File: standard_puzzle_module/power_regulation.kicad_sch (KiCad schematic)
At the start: 9 parts, among them J10 Screw_Terminal_01x02, U9 TSR2-2450

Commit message: chore: clean up
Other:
- title: Power input and regulation (12V to 5V) -> Power input and regulation
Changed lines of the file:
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@@
 	(paper "A4")
 	(title_block
-		(title "Power input and regulation (12V to 5V)")
+		(title "Power input and regulation")
 	)
 	(junction
@@
 	)
 	(junction
+		(at 101.6 87.63)
+		(diameter 0)
+		(color 0 0 0 0)
+	)
+	(junction
 		(at 147.32 82.55)
 		(diameter 0)
@@
 	(wire
 		(pts
-			(xy 101.6 82.55) (xy 101.6 92.71)
+			(xy 101.6 82.55) (xy 101.6 87.63)
 		)
 		(stroke
@@
 	(wire
 		(pts
+			(xy 101.6 87.63) (xy 101.6 92.71)
+		)
+		(stroke
+			(width 0)
+			(type default)
+		)
+	)
+	(wire
+		(pts
 			(xy 147.32 93.98) (xy 147.32 106.68)
 		)
@@
 	)
 	(label "Power input and regulation (12V to 5V)"
-		(at 123.19 73.66 0)
+		(at 123.19 71.12 0)
 		(effects
 			(font
 				(size 1.778 1.778)
-			)
-			(justify left bottom)
-		)
-	)
-	(label "+12V"
-		(at 101.6 90.17 0)
-		(effects
-			(font
-				(size 1.27 1.27)
-			)
-			(justify left bottom)
-		)
-	)
-	(label "GND"
-		(at 101.6 99.06 0)
-		(effects
-			(font
-				(size 1.27 1.27)
 			)
 			(justify left bottom)
@@
 					(unit 1)
 				)
+			)
+		)
+	)
+	(symbol
+		(lib_id "power:+12V")
+		(at 101.6 87.63 0)
+		(unit 1)
+		(body_style 1)
+		(exclude_from_sim no)
+		(in_bom yes)
+		(on_board yes)
+		(in_pos_files yes)
+		(dnp no)
+		(fields_autoplaced yes)
+		(property "Reference" "#PWR04"
+			(at 101.6 91.44 0)
+			(hide yes)
+			(show_name no)
+			(do_not_autoplace no)
+			(effects
+				(font
+					(size 1.27 1.27)
+				)
+			)
+		)
+		(property "Value" "+12V"
+			(at 101.6 82.55 0)
+			(show_name no)
+			(do_not_autoplace no)
+			(effects
+				(font
+					(size 1.27 1.27)
+				)
+			)
+		)
+		(property "Footprint" ""
+			(at 101.6 87.63 0)
+			(hide yes)
+			(show_name no)
+			(do_not_autoplace no)
+			(effects
+				(font
+					(size 1.27 1.27)
+				)
+			)
+		)
+		(property "Datasheet" ""
+			(at 101.6 87.63 0)
+			(hide yes)
+			(show_name no)
+			(do_not_autoplace no)
+			(effects
+				(font
+					(size 1.27 1.27)
+				)
+			)
+		)
+		(property "Description" "Power symbol creates a global label with name \"+12V\""
+			(at 101.6 87.63 0)
+			(hide yes)
+			(show_name no)
+			(do_not_autoplace no)
+			(effects
+				(font
+					(size 1.27 1.27)
+				)
+			)
+		)
+		(pin "1"
+		)
+		(instances
+			(project "standard_puzzle_box"
+				(path "/13314f97-080e-4924-a8fe-b4d224920625/84527307-db04-4e9a-b4c6-f367c646187b"
+					(reference "#PWR04")
+					(unit 1)
+				)

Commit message: feat: unscrew git tracking
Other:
- moved on the sheet: C15, C16
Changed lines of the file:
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@@
+	)
+	(junction
+		(at 191.77 82.55)
+		(diameter 0)
+		(color 0 0 0 0)
+	)
+	(junction
+		(at 135.89 106.68)
+		(diameter 0)
+		(color 0 0 0 0)
+	)
+	(junction
+		(at 182.88 106.68)
+		(diameter 0)
+		(color 0 0 0 0)
 	)
 	(junction
@@
 	)
 	(junction
-		(at 135.89 106.68)
-		(diameter 0)
-		(color 0 0 0 0)
-	)
-	(junction
-		(at 182.88 106.68)
-		(diameter 0)
-		(color 0 0 0 0)
-	)
-	(junction
 		(at 101.6 87.63)
 		(diameter 0)
@@
 	)
 	(junction
+		(at 191.77 106.68)
+		(diameter 0)
+		(color 0 0 0 0)
+	)
+	(junction
 		(at 182.88 82.55)
 		(diameter 0)
@@
 	)
 	(junction
-		(at 191.77 82.55)
-		(diameter 0)
-		(color 0 0 0 0)
-	)
-	(junction
 		(at 115.57 106.68)
 		(diameter 0)
@@
 	)
 	(junction
-		(at 191.77 106.68)
-		(diameter 0)
-		(color 0 0 0 0)
-	)
-	(junction
 		(at 168.91 106.68)
 		(diameter 0)
@@
 	(wire
 		(pts
-			(xy 191.77 102.87) (xy 191.77 106.68)
+			(xy 191.77 101.6) (xy 191.77 106.68)
 		)
 		(stroke
@@
 	(wire
 		(pts
-			(xy 182.88 92.71) (xy 182.88 106.68)
+			(xy 182.88 93.98) (xy 182.88 106.68)
 		)
 		(stroke
@@
 	(wire
 		(pts
-			(xy 191.77 95.25) (xy 191.77 82.55)
+			(xy 191.77 93.98) (xy 191.77 82.55)
 		)
 		(stroke
@@
 	(wire
 		(pts
-			(xy 182.88 82.55) (xy 182.88 85.09)
+			(xy 182.88 82.55) (xy 182.88 86.36)
 		)
 		(stroke
@@
 	(symbol
 		(lib_id "Device:C_Polarized")
-		(at 182.88 88.9 0)
+		(at 182.88 90.17 0)
 		(unit 1)
 		(body_style 1)
@@
 		(fields_autoplaced yes)
 		(property "Reference" "C15"
-			(at 186.69 86.7409 0)
+			(at 186.69 88.0109 0)
 			(show_name no)
 			(do_not_autoplace no)
@@
 		)
 		(property "Value" "47uF"
-			(at 186.69 89.2809 0)
+			(at 186.69 90.5509 0)
 			(show_name no)
 			(do_not_autoplace no)
@@
 		)
 		(property "Footprint" ""
-			(at 183.8452 92.71 0)
+			(at 183.8452 93.98 0)
 			(hide yes)
 			(show_name no)
@@
 		)
 		(property "Datasheet" ""
-			(at 182.88 88.9 0)
+			(at 182.88 90.17 0)
 			(hide yes)
 			(show_name no)
@@
 		)
 		(property "Description" "Polarized capacitor"
-			(at 182.88 88.9 0)
+			(at 182.88 90.17 0)
 			(hide yes)
 			(show_name no)
@@
 	(symbol
 		(lib_id "Device:C")
-		(at 191.77 99.06 0)
+		(at 191.77 97.79 0)
 		(unit 1)
 		(body_style 1)
@@
 		(fields_autoplaced yes)
 		(property "Reference" "C16"
-			(at 195.58 97.7899 0)
+			(at 195.58 96.5199 0)
 			(show_name no)
 			(do_not_autoplace no)
@@
 		)
 		(property "Value" "100nF"
-			(at 195.58 100.3299 0)
+			(at 195.58 99.0599 0)
 			(show_name no)
 			(do_not_autoplace no)
@@
 		)
 		(property "Footprint" ""
-			(at 192.7352 102.87 0)
+			(at 192.7352 101.6 0)
 			(hide yes)
 			(show_name no)
@@
 		)
 		(property "Datasheet" ""
-			(at 191.77 99.06 0)
+			(at 191.77 97.79 0)
 			(hide yes)
 			(show_name no)
@@
 		)
 		(property "Description" "Unpolarized capacitor"
-			(at 191.77 99.06 0)
-			(hide yes)
-			(show_name no)
+			(at 191.77 97.79 0)
+			(hide yes)
+			(show_name no)

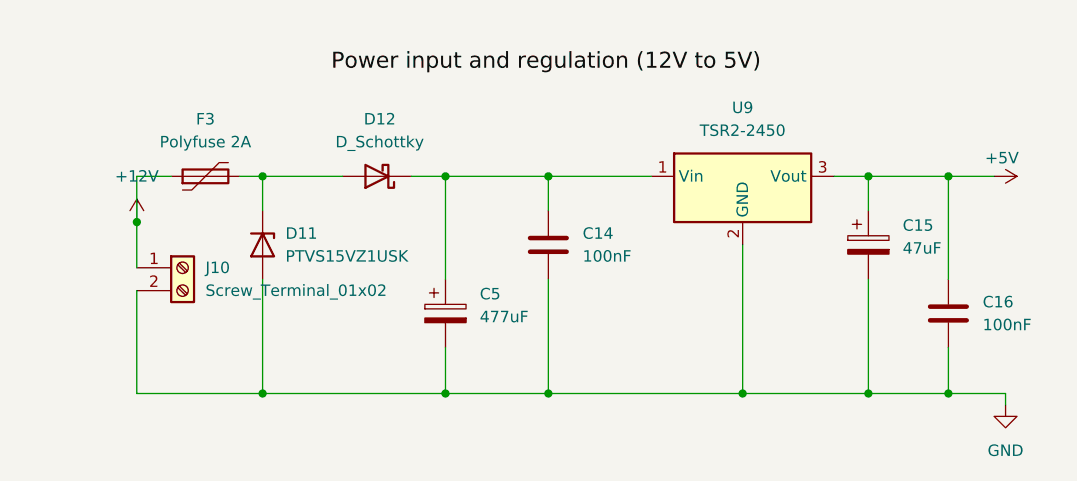
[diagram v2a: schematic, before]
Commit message: feat: clean up schematic references and run clean annotation
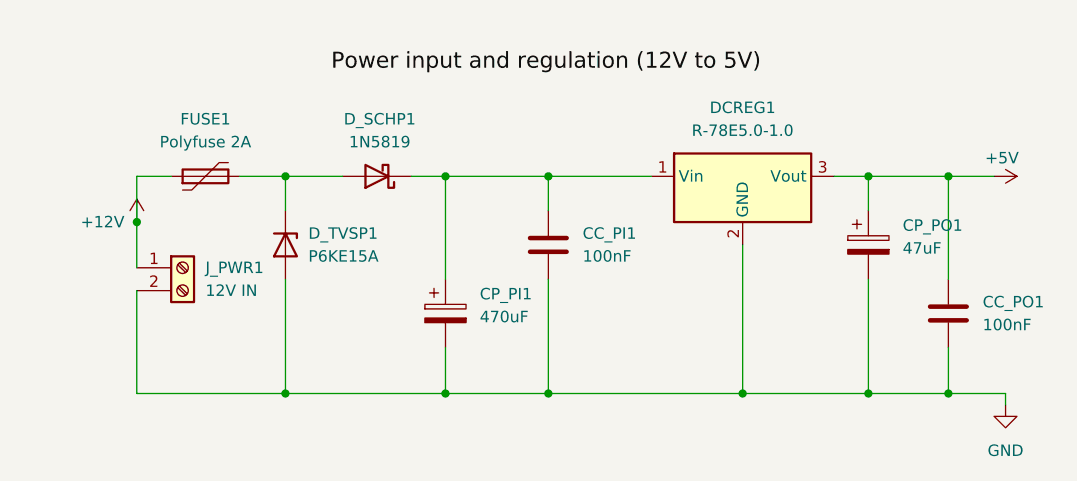
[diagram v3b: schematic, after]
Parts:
- CC_PI1: renamed from C14; footprint (none) -> Capacitor_THT:C_Disc_D5.0mm_W2.5mm_P5.00mm
- CC_PO1: renamed from C16; footprint (none) -> Capacitor_THT:C_Disc_D5.0mm_W2.5mm_P5.00mm
- CP_PI1: renamed from C5; value 477uF -> 470uF; footprint (none) -> Capacitor_THT:CP_Radial_D10.0mm_P5.00mm
- CP_PO1: renamed from C15; footprint (none) -> Capacitor_THT:CP_Radial_D6.3mm_P2.50mm
- DCREG1: renamed from U9; value TSR2-2450 -> R-78E5.0-1.0; footprint Converter_DCDC:Converter_DCDC_TRACO_TSR2-xxxx_THT -> Converter_DCDC:Converter_DCDC_RECOM_R-78E-0.5_THT
- D_SCHP1: renamed from D12; value D_Schottky -> 1N5819; footprint (none) -> Diode_THT:D_DO-35_SOD27_P7.62mm_Horizontal
- D_TVSP1: renamed from D11; value PTVS15VZ1USK -> P6KE15A; footprint Diode_SMD:Nexperia_DSN1608-2_1.6x0.8mm -> Diode_THT:D_DO-15_P12.70mm_Horizontal
- FUSE1: renamed from F3; footprint (none) -> Fuse:Fuse_BelFuse_0ZRE0040FF_L11.5mm_W3.8mm
- J_PWR1: renamed from J10; value Screw_Terminal_01x02 -> 12V IN; footprint (none) -> TerminalBlock_Phoenix:TerminalBlock_Phoenix_MKDS-1,5-2-5.08_1x02_P5.08mm_Horizontal
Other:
- moved on the sheet: D_TVSP1
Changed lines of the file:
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@@
-	)
-	(junction
-		(at 115.57 82.55)
-		(diameter 0)
-		(color 0 0 0 0)
 	)
 	(junction
@@
 	)
 	(junction
-		(at 115.57 106.68)
+		(at 118.11 106.68)
 		(diameter 0)
 		(color 0 0 0 0)
@@
 		(color 0 0 0 0)
 	)
+	(junction
+		(at 118.11 82.55)
+		(diameter 0)
+		(color 0 0 0 0)
+	)
 	(wire
 		(pts
@@
 	(wire
 		(pts
-			(xy 113.03 82.55) (xy 115.57 82.55)
-		)
-		(stroke
-			(width 0)
-			(type default)
-		)
-	)
-	(wire
-		(pts
-			(xy 115.57 106.68) (xy 135.89 106.68)
+			(xy 113.03 82.55) (xy 118.11 82.55)
 		)
 		(stroke
@@
 	(wire
 		(pts
-			(xy 101.6 106.68) (xy 115.57 106.68)
+			(xy 101.6 106.68) (xy 118.11 106.68)
 		)
 		(stroke
@@
 	(wire
 		(pts
-			(xy 115.57 93.98) (xy 115.57 106.68)
+			(xy 118.11 93.98) (xy 118.11 106.68)
 		)
 		(stroke
@@
 	(wire
 		(pts
+			(xy 118.11 82.55) (xy 124.46 82.55)
+		)
+		(stroke
+			(width 0)
+			(type default)
+		)
+	)
+	(wire
+		(pts
 			(xy 168.91 106.68) (xy 182.88 106.68)
 		)
@@
 	(wire
 		(pts
-			(xy 115.57 82.55) (xy 115.57 86.36)
+			(xy 118.11 82.55) (xy 118.11 86.36)
 		)
 		(stroke
@@
 	(wire
 		(pts
-			(xy 115.57 82.55) (xy 124.46 82.55)
+			(xy 118.11 106.68) (xy 135.89 106.68)
 		)
 		(stroke
@@
 		(dnp no)
 		(fields_autoplaced yes)
-		(property "Reference" "C14"
+		(property "Reference" "CC_PI1"
 			(at 151.13 88.8999 0)
 			(show_name no)
@@
 			)
 		)
-		(property "Footprint" ""
+		(property "Footprint" "Capacitor_THT:C_Disc_D5.0mm_W2.5mm_P5.00mm"
 			(at 148.2852 93.98 0)
 			(hide yes)
@@
 			(project "standard_puzzle_box"
 				(path "/13314f97-080e-4924-a8fe-b4d224920625/84527307-db04-4e9a-b4c6-f367c646187b"
-					(reference "C14")
+					(reference "CC_PI1")
 					(unit 1)
 				)
@@
 		(dnp no)
 		(fields_autoplaced yes)
-		(property "Reference" "C15"
+		(property "Reference" "CP_PO1"
 			(at 186.69 88.0109 0)
 			(show_name no)
@@
 			)
 		)
-		(property "Footprint" ""
+		(property "Footprint" "Capacitor_THT:CP_Radial_D6.3mm_P2.50mm"
 			(at 183.8452 93.98 0)
 			(hide yes)
@@
 			(project "standard_puzzle_box"
 				(path "/13314f97-080e-4924-a8fe-b4d224920625/84527307-db04-4e9a-b4c6-f367c646187b"
-					(reference "C15")
+					(reference "CP_PO1")
 					(unit 1)
 				)
@@
 	(symbol
 		(lib_id "Diode:PTVS15VZ1USK")
-		(at 115.57 90.17 270)
+		(at 118.11 90.17 270)
 		(unit 1)
 		(body_style 1)
@@
 		(dnp no)
 		(fields_autoplaced yes)
-		(property "Reference" "D11"
-			(at 118.11 88.8999 90)
-			(show_name no)
-			(do_not_autoplace no)
-			(effects
-				(font
-					(size 1.27 1.27)
-				)
-				(justify left)
-			)
-		)
-		(property "Value" "PTVS15VZ1USK"
-			(at 118.11 91.4399 90)
-			(show_name no)
-			(do_not_autoplace no)
-			(effects
-				(font
-					(size 1.27 1.27)
-				)
-				(justify left)
-			)
-		)
-		(property "Footprint" "Diode_SMD:Nexperia_DSN1608-2_1.6x0.8mm"
-			(at 111.125 90.17 0)
+		(property "Reference" "D_TVSP1"
+			(at 120.65 88.8999 90)
+			(show_name no)
+			(do_not_autoplace no)
+			(effects
+				(font
+					(size 1.27 1.27)
+				)
+				(justify left)
+			)
+		)
+		(property "Value" "P6KE15A"
+			(at 120.65 91.4399 90)
+			(show_name no)
+			(do_not_autoplace no)
+			(effects
+				(font
+					(size 1.27 1.27)
+				)
+				(justify left)
+			)
+		)
+		(property "Footprint" "Diode_THT:D_DO-15_P12.70mm_Horizontal"
+			(at 113.665 90.17 0)
 			(hide yes)
 			(show_name no)
@@
 		)
 		(property "Datasheet" "https://assets.nexperia.com/documents/data-sheet/PTVS15VZ1USK.pdf"
-			(at 115.57 90.17 0)
+			(at 118.11 90.17 0)
 			(hide yes)
 			(show_name no)
@@
 		)
 		(property "Description" "15V, 1900W TVS unidirectional diode, DSN1608-2"
-			(at 115.57 90.17 0)
+			(at 118.11 90.17 0)
 			(hide yes)
 			(show_name no)
@@
 			(project "standard_puzzle_box"
 				(path "/13314f97-080e-4924-a8fe-b4d224920625/84527307-db04-4e9a-b4c6-f367c646187b"
-					(reference "D11")
+					(reference "D_TVSP1")
 					(unit 1)
 				)
@@
 		(in_pos_files yes)
 		(dnp no)
-		(fields_autoplaced yes)
 		(property "Reference" "#PWR04"
 			(at 101.6 91.44 0)
@@
 		)
 		(property "Value" "+12V"
-			(at 101.6 82.55 0)
+			(at 97.79 87.63 0)
 			(show_name no)
 			(do_not_autoplace no)
@@
 		(dnp no)
 		(fields_autoplaced yes)
-		(property "Reference" "U9"
+		(property "Reference" "DCREG1"
 			(at 168.91 74.93 0)
 			(show_name no)
@@
 			)
 		)
-		(property "Value" "TSR2-2450"
+		(property "Value" "R-78E5.0-1.0"
 			(at 168.91 77.47 0)
 			(show_name no)
@@
 			)
 		)
-		(property "Footprint" "Converter_DCDC:Converter_DCDC_TRACO_TSR2-xxxx_THT"
+		(property "Footprint" "Converter_DCDC:Converter_DCDC_RECOM_R-78E-0.5_THT"
 			(at 168.91 91.186 0)
 			(hide yes)
@@
 			(project "standard_puzzle_box"
 				(path "/13314f97-080e-4924-a8fe-b4d224920625/84527307-db04-4e9a-b4c6-f367c646187b"
-					(reference "U9")
+					(reference "DCREG1")
 					(unit 1)
 				)
@@
 		(dnp no)
 		(fields_autoplaced yes)
-		(property "Reference" "C16"
+		(property "Reference" "CC_PO1"
 			(at 195.58 96.5199 0)
 			(show_name no)
@@
 			)
 		)
-		(property "Footprint" ""
+		(property "Footprint" "Capacitor_THT:C_Disc_D5.0mm_W2.5mm_P5.00mm"
 			(at 192.7352 101.6 0)
 			(hide yes)
@@
 			(project "standard_puzzle_box"
 				(path "/13314f97-080e-4924-a8fe-b4d224920625/84527307-db04-4e9a-b4c6-f367c646187b"
-					(reference "C16")
+					(reference "CC_PO1")
 					(unit 1)
 				)
@@
 		(dnp no)
 		(fields_autoplaced yes)
-		(property "Reference" "D12"
+		(property "Reference" "D_SCHP1"
 			(at 128.5875 76.2 0)
 			(show_name no)
@@
 			)
 		)
-		(property "Value" "D_Schottky"
+		(property "Value" "1N5819"
 			(at 128.5875 78.74 0)
 			(show_name no)
@@
 			)
 		)
-		(property "Footprint" ""
+		(property "Footprint" "Diode_THT:D_DO-35_SOD27_P7.62mm_Horizontal"
 			(at 128.27 82.55 0)
 			(hide yes)
@@
 			(project "standard_puzzle_box"
 				(path "/13314f97-080e-4924-a8fe-b4d224920625/84527307-db04-4e9a-b4c6-f367c646187b"
-					(reference "D12")
+					(reference "D_SCHP1")
 					(unit 1)
 				)
@@
 		(dnp no)
 		(fields_autoplaced yes)
-		(property "Reference" "F3"
+		(property "Reference" "FUSE1"
 			(at 109.22 76.2 90)
 			(show_name no)
@@
 			)
 		)
-		(property "Footprint" ""
+		(property "Footprint" "Fuse:Fuse_BelFuse_0ZRE0040FF_L11.5mm_W3.8mm"
 			(at 114.3 81.28 0)
 			(hide yes)
@@
 			(project "standard_puzzle_box"
 				(path "/13314f97-080e-4924-a8fe-b4d224920625/84527307-db04-4e9a-b4c6-f367c646187b"
-					(reference "F3")
+					(reference "FUSE1")
 					(unit 1)
 				)
@@
 		(dnp no)
 		(fields_autoplaced yes)
-		(property "Reference" "J10"
+		(property "Reference" "J_PWR1"
 			(at 109.22 92.7099 0)
 			(show_name no)
@@
 			)
 		)
-		(property "Value" "Screw_Terminal_01x02"
+		(property "Value" "12V IN"
 			(at 109.22 95.2499 0)
 			(show_name no)
@@
 			)
 		)
-		(property "Footprint" ""
+		(property "Footprint" "TerminalBlock_Phoenix:TerminalBlock_Phoenix_MKDS-1,5-2-5.08_1x02_P5.08mm_Horizontal"
 			(at 106.68 92.71 0)
 			(hide yes)
@@
 			(project "standard_puzzle_box"
 				(path "/13314f97-080e-4924-a8fe-b4d224920625/84527307-db04-4e9a-b4c6-f367c646187b"
-					(reference "J10")
+					(reference "J_PWR1")
 					(unit 1)
 				)
@@
 		(dnp no)
 		(fields_autoplaced yes)
-		(property "Reference" "C5"
+		(property "Reference" "CP_PI1"
 			(at 139.7 95.6309 0)
 			(show_name no)
@@
 			)
 		)
-		(property "Value" "477uF"
+		(property "Value" "470uF"
 			(at 139.7 98.1709 0)
 			(show_name no)
@@
 			)
 		)
-		(property "Footprint" ""
+		(property "Footprint" "Capacitor_THT:CP_Radial_D10.0mm_P5.00mm"
 			(at 136.8552 101.6 0)
 			(hide yes)
@@
 			(project "standard_puzzle_box"
 				(path "/13314f97-080e-4924-a8fe-b4d224920625/84527307-db04-4e9a-b4c6-f367c646187b"
-					(reference "C5")
+					(reference "CP_PI1")
 					(unit 1)
 				)

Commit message: fix: run erc and fix errors and warnings
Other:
- note added: "Power input and regulation (12V to 5V)"

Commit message: feat: salvaging stuff after lossy crash
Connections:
- net +12V: now also CC_PI1.1, CP_PI1.1, DCREG1.1 (Vin), D_SCHP1.1 (K); no longer FUSE1.1, J_PWR1.1 (Pin_1)
- new net: FUSE1.1, J_PWR1.1 (Pin_1)
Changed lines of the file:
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@@
+	)
+	(junction
+		(at 152.4 82.55)
+		(diameter 0)
+		(color 0 0 0 0)
 	)
 	(junction
@@
 	)
 	(junction
-		(at 101.6 87.63)
+		(at 147.32 82.55)
 		(diameter 0)
 		(color 0 0 0 0)
@@
 	)
 	(junction
-		(at 147.32 82.55)
-		(diameter 0)
-		(color 0 0 0 0)
-	)
-	(junction
 		(at 198.12 106.68)
 		(diameter 0)
@@
 	(wire
 		(pts
+			(xy 147.32 82.55) (xy 152.4 82.55)
+		)
+		(stroke
+			(width 0)
+			(type default)
+		)
+	)
+	(wire
+		(pts
 			(xy 182.88 106.68) (xy 191.77 106.68)
 		)
@@
 	(wire
 		(pts
-			(xy 101.6 82.55) (xy 101.6 87.63)
-		)
-		(stroke
-			(width 0)
-			(type default)
-		)
-	)
-	(wire
-		(pts
-			(xy 147.32 82.55) (xy 154.94 82.55)
+			(xy 101.6 82.55) (xy 101.6 92.71)
 		)
 		(stroke
@@
 	(wire
 		(pts
-			(xy 101.6 87.63) (xy 101.6 92.71)
-		)
-		(stroke
-			(width 0)
-			(type default)
-		)
-	)
-	(wire
-		(pts
 			(xy 147.32 93.98) (xy 147.32 106.68)
 		)
@@
 		(pts
 			(xy 179.07 82.55) (xy 182.88 82.55)
+		)
+		(stroke
+			(width 0)
+			(type default)
+		)
+	)
+	(wire
+		(pts
+			(xy 152.4 82.55) (xy 154.94 82.55)
 		)
 		(stroke
@@
 	(symbol
 		(lib_id "power:+12V")
-		(at 101.6 87.63 0)
+		(at 152.4 82.55 0)
 		(unit 1)
 		(body_style 1)
@@
 		(dnp no)
 		(property "Reference" "#PWR04"
-			(at 101.6 91.44 0)
+			(at 152.4 86.36 0)
 			(hide yes)
 			(show_name no)
@@
 		)
 		(property "Value" "+12V"
-			(at 97.79 87.63 0)
+			(at 148.59 80.01 0)
 			(show_name no)
 			(do_not_autoplace no)
@@
 		)
 		(property "Footprint" ""
-			(at 101.6 87.63 0)
+			(at 152.4 82.55 0)
 			(hide yes)
 			(show_name no)
@@
 		)
 		(property "Datasheet" ""
-			(at 101.6 87.63 0)
+			(at 152.4 82.55 0)
 			(hide yes)
 			(show_name no)
@@
 		)
 		(property "Description" "Power symbol creates a global label with name \"+12V\""
-			(at 101.6 87.63 0)
-			(hide yes)
-			(show_name no)
+			(at 152.4 82.55 0)
+			(hide yes)
+			(show_name no)
